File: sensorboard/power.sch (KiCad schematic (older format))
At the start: 32 parts, among them J11 Conn_01x02_Male, U12 MAX40200AUK, U8 TPS63031

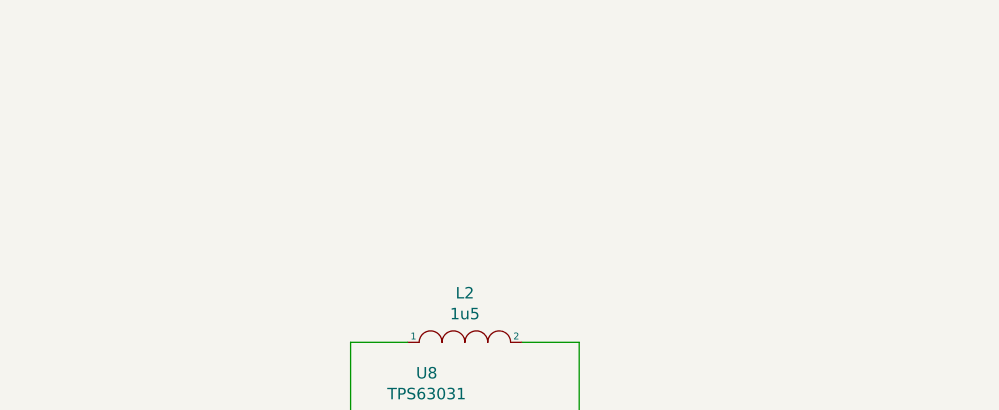
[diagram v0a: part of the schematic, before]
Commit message: Voltage divider setup
Voltage divider setup, removed unused components, CAN RX/TX empty for now (waiting for kiran)
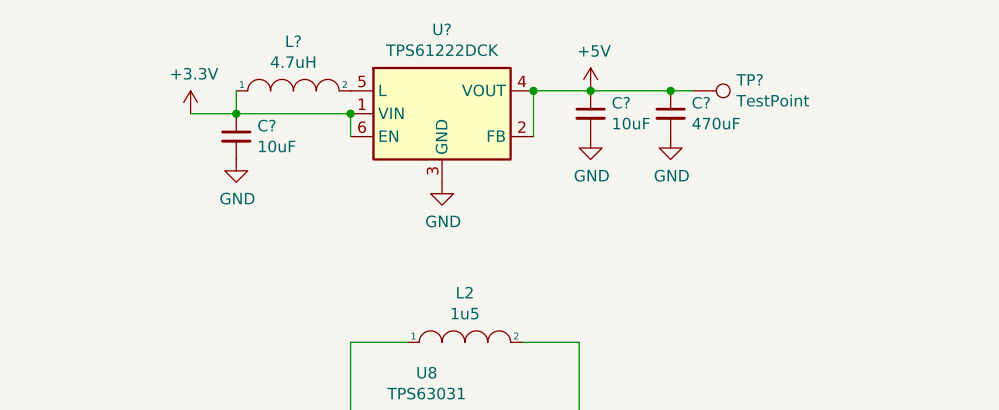
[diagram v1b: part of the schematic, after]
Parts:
- added C? (x2): 10uF, symbol Device:C_Small
- added C?: 470uF, symbol Device:C_Small
- added L?: 4.7uH, symbol pspice:INDUCTOR
- added TP?: TestPoint, symbol Connector:TestPoint
- added U?: TPS61222DCK, Package_TO_SOT_SMD:Texas_R-PDSO-G6, symbol Regulator_Switching:TPS61222DCK
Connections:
- net +3V3: now also C?.1, L?.1, U?.1 (VIN), U?.6 (EN)
- net GND: now also C?.2, C?.2, C?.2, U?.3 (GND)
- new net: L?.2, U?.5 (L)
- new net +5V: C?.1, C?.1, TP?.1, U?.2 (FB), U?.4 (VOUT)
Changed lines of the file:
@@
 Wire Wire Line
 	3300 3850 3200 3850
+$Comp
+L Regulator_Switching:TPS61222DCK U?
+U 1 1 618C461B
+P 5800 2200
+F 0 "U?" H 5800 2567 50  0000 C CNN
+F 1 "TPS61222DCK" H 5800 2476 50  0000 C CNN
+F 2 "Package_TO_SOT_SMD:Texas_R-PDSO-G6" H 5800 1400 50  0001 C CNN
+F 3 "http://www.ti.com/lit/ds/symlink/tps61220.pdf" H 5800 2050 50  0001 C CNN
+	1    5800 2200
+	1    0    0    -1
+$EndComp
+Wire Wire Line
+	5400 2200 4900 2200
+$Comp
+L pspice:INDUCTOR L?
+U 1 1 618CA5D3
+P 5150 2100
+F 0 "L?" H 5150 2315 50  0000 C CNN
+F 1 "4.7uH" H 5150 2224 50  0000 C CNN
+F 2 "" H 5150 2100 50  0001 C CNN
+F 3 "~" H 5150 2100 50  0001 C CNN
+	1    5150 2100
+	1    0    0    -1
+$EndComp
+Wire Wire Line
+	5400 2300 5400 2200
+Connection ~ 5400 2200
+Wire Wire Line
+	4900 2100 4900 2200
+Connection ~ 4900 2200
+Wire Wire Line
+	4900 2200 4700 2200
+$Comp
+L Device:C_Small C?
+U 1 1 618D23E9
+P 4900 2300
+F 0 "C?" H 4992 2346 50  0000 L CNN
+F 1 "10uF" H 4992 2255 50  0000 L CNN
+F 2 "" H 4900 2300 50  0001 C CNN
+F 3 "~" H 4900 2300 50  0001 C CNN
+	1    4900 2300
+	1    0    0    -1
+$EndComp
+$Comp
+L power:GND #PWR?
+U 1 1 618D297D
+P 4900 2400
+F 0 "#PWR?" H 4900 2150 50  0001 C CNN
+F 1 "GND" H 4905 2227 50  0000 C CNN
+F 2 "" H 4900 2400 50  0001 C CNN
+F 3 "" H 4900 2400 50  0001 C CNN
+	1    4900 2400
+	1    0    0    -1
+$EndComp
+$Comp
+L power:GND #PWR?
+U 1 1 618D2FC0
+P 5800 2500
+F 0 "#PWR?" H 5800 2250 50  0001 C CNN
+F 1 "GND" H 5805 2327 50  0000 C CNN
+F 2 "" H 5800 2500 50  0001 C CNN
+F 3 "" H 5800 2500 50  0001 C CNN
+	1    5800 2500
+	1    0    0    -1
+$EndComp
+Wire Wire Line
+	6200 2100 6200 2300
+Wire Wire Line
+	6200 2100 6450 2100
+Connection ~ 6200 2100
+$Comp
+L power:+5V #PWR?
+U 1 1 618E8869
+P 6450 2100
+F 0 "#PWR?" H 6450 1950 50  0001 C CNN
+F 1 "+5V" H 6465 2273 50  0000 C CNN
+F 2 "" H 6450 2100 50  0001 C CNN
+F 3 "" H 6450 2100 50  0001 C CNN
+	1    6450 2100
+	1    0    0    -1
+$EndComp
+$Comp
+L Connector:TestPoint TP?
+U 1 1 618E9040
+P 6900 2100
+F 0 "TP?" V 6854 2288 50  0000 L CNN
+F 1 "TestPoint" V 6945 2288 50  0000 L CNN
+F 2 "" H 7100 2100 50  0001 C CNN
+F 3 "~" H 7100 2100 50  0001 C CNN
+	1    6900 2100
+	0    1    1    0
+$EndComp
+Connection ~ 6450 2100
+$Comp
+L analogue-cache:+3.3V #PWR?
+U 1 1 618E9917
+P 4700 2200
+F 0 "#PWR?" H 4700 2050 50  0001 C CNN
+F 1 "+3.3V" H 4715 2373 50  0000 C CNN
+F 2 "" H 4700 2200 50  0001 C CNN
+F 3 "" H 4700 2200 50  0001 C CNN
+	1    4700 2200
+	1    0    0    -1
+$EndComp
+$Comp
+L Device:C_Small C?
+U 1 1 618EAC0B
+P 6450 2200
+F 0 "C?" H 6542 2246 50  0000 L CNN
+F 1 "10uF" H 6542 2155 50  0000 L CNN
+F 2 "" H 6450 2200 50  0001 C CNN
+F 3 "~" H 6450 2200 50  0001 C CNN
+	1    6450 2200
+	1    0    0    -1
+$EndComp
+$Comp
+L power:GND #PWR?
+U 1 1 618EEBE4
+P 6450 2300
+F 0 "#PWR?" H 6450 2050 50  0001 C CNN
+F 1 "GND" H 6455 2127 50  0000 C CNN
+F 2 "" H 6450 2300 50  0001 C CNN
+F 3 "" H 6450 2300 50  0001 C CNN
+	1    6450 2300
+	1    0    0    -1
+$EndComp
+$Comp
+L power:GND #PWR?
+U 1 1 618FEE0C
+P 6800 2300
+F 0 "#PWR?" H 6800 2050 50  0001 C CNN
+F 1 "GND" H 6805 2127 50  0000 C CNN
+F 2 "" H 6800 2300 50  0001 C CNN
+F 3 "" H 6800 2300 50  0001 C CNN
+	1    6800 2300
+	1    0    0    -1
+$EndComp
+$Comp
+L Device:C_Small C?
+U 1 1 618FEE06
+P 6800 2200
+F 0 "C?" H 6892 2246 50  0000 L CNN
+F 1 "470uF" H 6892 2155 50  0000 L CNN
+F 2 "" H 6800 2200 50  0001 C CNN
+F 3 "~" H 6800 2200 50  0001 C CNN
+	1    6800 2200
+	1    0    0    -1
+$EndComp
+Wire Wire Line
+	6900 2100 6800 2100
+Wire Wire Line
+	6450 2100 6800 2100
+Connection ~ 6800 2100
 $EndSCHEMATC
